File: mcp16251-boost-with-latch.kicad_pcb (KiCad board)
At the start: 2 copper layers, 28 parts, among them J1 THT_Castellated, J2 THT_Castellated, J3 THT_Castellated, J4 SMD_pad, J5 SMD_pad, J6 SMD_pad, J7 SMD_pad, J8 SMD_pad, J9 JST_PH_Header, Q1 Q_PMOS_GSD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

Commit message: Set design rules
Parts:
- moved R4 17.3 mm to (137.2, 96.5)
- moved R5 13.0 mm to (137.2, 101.6)
- moved SW2 13.0 mm to (134.6, 106.7)
- moved Q2 13.0 mm to (142.2, 101.6)
- moved R2 10.8 mm to (170.2, 87.8)
- moved R3 10.8 mm to (170.2, 94.0)
- moved RV1 10.8 mm to (172.7, 91.4)
- moved R1 10.2 mm to (139.7, 78.7)
- moved Q1 10.2 mm to (134.6, 78.7)
- moved C4 5.68 mm to (149.9, 85.5)
- moved C3 5.68 mm to (147.3, 85.5)
- turned U1 to 90 degrees
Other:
- net class Default: clearance 0.2 -> 0.2032; trace_width 0.25 -> 0.2032; via_dia 0.8 -> 0.6604; via_drill 0.4 -> 0.3302
- rule pad_to_mask_clearance: 0.051 -> 0.0508
- rule solder_mask_min_width: 0.25 -> 0.1778
- rule trace_clearance: 0.2 -> 0.2032
- rule trace_min: 0.2 -> 0.1778
- rule via_min_drill: 0.3 -> 0.3048
- rule via_min_size: 0.4 -> 0.6096
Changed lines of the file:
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@@
   )
   (layers
-    (0 F.Cu signal)
-    (31 B.Cu signal)
-    (32 B.Adhes user)
-    (33 F.Adhes user)
+    (0 F.Cu mixed)
+    (31 B.Cu mixed)
     (34 B.Paste user)
     (35 F.Paste user)
@@
   )
   (setup
-    (last_trace_width 0.25)
-    (trace_clearance 0.2)
+    (last_trace_width 0.2032)
+    (trace_clearance 0.2032)
     (zone_clearance 0.508)
     (zone_45_only no)
-    (trace_min 0.2)
+    (trace_min 0.1778)
     (segment_width 0.2)
     (edge_width 0.15)
-    (via_size 0.8)
-    (via_drill 0.4)
-    (via_min_size 0.4)
-    (via_min_drill 0.3)
+    (via_size 0.6604)
+    (via_drill 0.3302)
+    (via_min_size 0.6096)
+    (via_min_drill 0.3048)
     (uvia_size 0.3)
     (uvia_drill 0.1)
@@
     (pad_size 1.524 1.524)
     (pad_drill 0.762)
-    (pad_to_mask_clearance 0.051)
-    (solder_mask_min_width 0.25)
+    (pad_to_mask_clearance 0.0508)
+    (solder_mask_min_width 0.1778)
     (aux_axis_origin 0 0)
-    (visible_elements FFFFFF7F)
+    (visible_elements FFFFF77F)
     (pcbplotparams
       (layerselection 0x010fc_ffffffff)
@@
   (net 13 "Net-(SW1-Pad3)")
   (net_class Default "This is the default net class."
-    (clearance 0.2)
-    (trace_width 0.25)
-    (via_dia 0.8)
-    (via_drill 0.4)
+    (clearance 0.2032)
+    (trace_width 0.2032)
+    (via_dia 0.6604)
+    (via_drill 0.3302)
     (uvia_dia 0.3)
     (uvia_drill 0.1)
@@
   )
   (module MCP16251_module:R_1206_HS (layer F.Cu)
-    (at 142.24 88.01 270)
+    (at 147.32 85.47 270)
     (descr "Resistor SMD 1206, reflow soldering, Vishay (see dcrcw.pdf)")
     (tags "resistor 1206")
@@
   )
   (module MCP16251_module:R_1206_HS (layer F.Cu)
-    (at 144.78 88.01 270)
+    (at 149.86 85.47 270)
     (descr "Resistor SMD 1206, reflow soldering, Vishay (see dcrcw.pdf)")
     (tags "resistor 1206")
@@
   )
   (module MCP16251_module:SOT-23_HS (layer F.Cu)
-    (at 144.78 78.74 180)
+    (at 134.62 78.74 180)
     (descr "SOT-23, Standard")
     (tags SOT-23)
@@
   )
   (module MCP16251_module:SOT-23_HS (layer F.Cu)
-    (at 154.94 99.06)
+    (at 142.24 101.6)
     (descr "SOT-23, Standard")
     (tags SOT-23)
@@
   )
   (module MCP16251_module:R_0805_HS (layer F.Cu)
-    (at 149.86 78.74 270)
+    (at 139.7 78.74 270)
     (descr "Resistor SMD 0805, reflow soldering, Vishay (see dcrcw.pdf)")
     (tags "resistor 0805")
@@
   )
   (module MCP16251_module:R_0805_HS (layer F.Cu)
-    (at 162.56 80.13 270)
+    (at 170.18 87.75 270)
     (descr "Resistor SMD 0805, reflow soldering, Vishay (see dcrcw.pdf)")
     (tags "resistor 0805")
@@
   )
   (module MCP16251_module:R_0805_HS (layer F.Cu)
-    (at 162.56 86.36 270)
+    (at 170.18 93.98 270)
     (descr "Resistor SMD 0805, reflow soldering, Vishay (see dcrcw.pdf)")
     (tags "resistor 0805")
@@
   )
   (module MCP16251_module:R_0805_HS (layer F.Cu)
-    (at 152.666 88.961001)
+    (at 137.16 96.52)
     (descr "Resistor SMD 0805, reflow soldering, Vishay (see dcrcw.pdf)")
     (tags "resistor 0805")
@@
   )
   (module MCP16251_module:R_0805_HS (layer F.Cu)
-    (at 149.86 99.06)
+    (at 137.16 101.6)
     (descr "Resistor SMD 0805, reflow soldering, Vishay (see dcrcw.pdf)")
     (tags "resistor 0805")
@@
   )
   (module MCP16251_module:Conn_01x03_small (layer F.Cu)
-    (at 165.1 83.82)
+    (at 172.72 91.44)
     (fp_text reference RV1 (at 1.905 0 90) (layer F.SilkS)
       (effects (font (size 1 1) (thickness 0.15)))
@@
   )
   (module Buttons_Switches_SMD:SW_SPST_TL3342 (layer F.Cu)
-    (at 147.32 104.14)
+    (at 134.62 106.68)
     (descr "Low-profile SMD Tactile Switch, https://www.e-switch.com/system/asset/product_line/data_sheet/165/TL3342.pdf")
     (tags "SPST Tactile Switch")
@@
   )
   (module MCP16251_module:SOT-23-6_HS (layer F.Cu)
-    (at 156.18 84.77)
+    (at 156.18 84.77 90)
     (descr "6-pin SOT-23 package")
     (tags SOT-23-6)
     (attr smd)
-    (fp_text reference U1 (at 0 -2.54) (layer F.SilkS)
-      (effects (font (size 1 1) (thickness 0.15)))
-    )
-    (fp_text value MCP16251T (at 0 2.9) (layer F.Fab) hide
+    (fp_text reference U1 (at 0 -2.54 90) (layer F.SilkS)
+      (effects (font (size 1 1) (thickness 0.15)))
+    )
+    (fp_text value MCP16251T (at 0 2.9 90) (layer F.Fab) hide
       (effects (font (size 1 1) (thickness 0.15)))
     )
@@
     (fp_line (start 0.9 -1.61) (end -1.55 -1.61) (layer F.SilkS) (width 0.12))
     (fp_line (start -0.9 1.61) (end 0.9 1.61) (layer F.SilkS) (width 0.12))
-    (fp_text user %R (at 0 0 90) (layer F.Fab)
-      (effects (font (size 0.5 0.5) (thickness 0.075)))
-    )
-    (pad 5 smd roundrect (at 1.3 0) (size 1.46 0.65) (layers F.Cu F.Paste F.Mask) (roundrect_rratio 0.25)
+    (fp_text user %R (at 0 0 180) (layer F.Fab)
+      (effects (font (size 0.5 0.5) (thickness 0.075)))
+    )
+    (pad 5 smd roundrect (at 1.3 0 90) (size 1.46 0.65) (layers F.Cu F.Paste F.Mask) (roundrect_rratio 0.25)
       (net 1 VCC))
-    (pad 6 smd roundrect (at 1.3 -0.95) (size 1.46 0.65) (layers F.Cu F.Paste F.Mask) (roundrect_rratio 0.25)
+    (pad 6 smd roundrect (at 1.3 -0.95 90) (size 1.46 0.65) (layers F.Cu F.Paste F.Mask) (roundrect_rratio 0.25)
       (net 3 VBAT))
-    (pad 4 smd roundrect (at 1.3 0.95) (size 1.46 0.65) (layers F.Cu F.Paste F.Mask) (roundrect_rratio 0.25)
+    (pad 4 smd roundrect (at 1.3 0.95 90) (size 1.46 0.65) (layers F.Cu F.Paste F.Mask) (roundrect_rratio 0.25)
       (net 10 "Net-(R2-Pad2)"))
-    (pad 3 smd roundrect (at -1.3 0.95) (size 1.46 0.65) (layers F.Cu F.Paste F.Mask) (roundrect_rratio 0.25)
+    (pad 3 smd roundrect (at -1.3 0.95 90) (size 1.46 0.65) (layers F.Cu F.Paste F.Mask) (roundrect_rratio 0.25)
       (net 3 VBAT))
-    (pad 2 smd roundrect (at -1.3 0) (size 1.46 0.65) (layers F.Cu F.Paste F.Mask) (roundrect_rratio 0.25)
-      (net 2 GND))
-    (pad 1 smd roundrect (at -1.3 -0.95) (size 1.46 0.65) (layers F.Cu F.Paste F.Mask) (roundrect_rratio 0.25)
+    (pad 2 smd roundrect (at -1.3 0 90) (size 1.46 0.65) (layers F.Cu F.Paste F.Mask) (roundrect_rratio 0.25)
+      (net 2 GND))
+    (pad 1 smd roundrect (at -1.3 -0.95 90) (size 1.46 0.65) (layers F.Cu F.Paste F.Mask) (roundrect_rratio 0.25)
       (net 7 "Net-(L1-Pad2)"))
     (model ${KISYS3DMOD}/TO_SOT_Packages_SMD.3dshapes/SOT-23-6.wrl

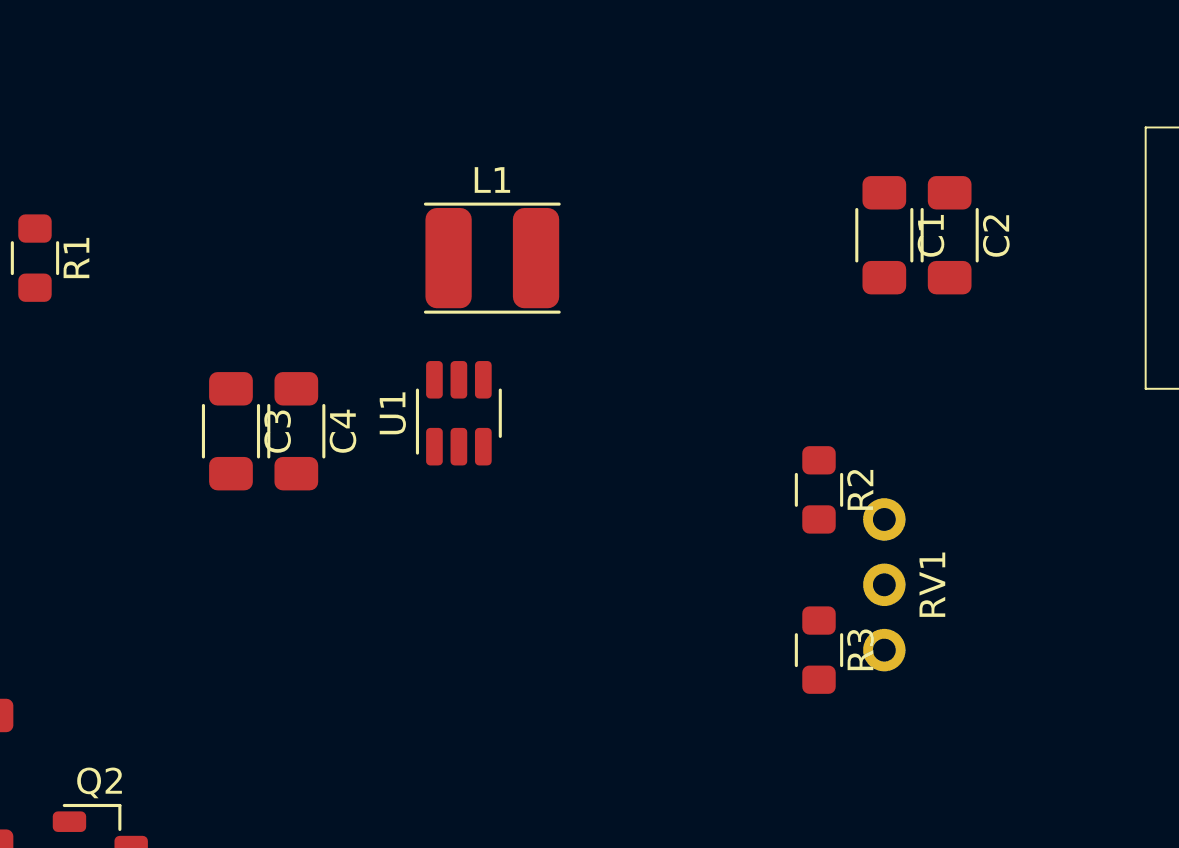
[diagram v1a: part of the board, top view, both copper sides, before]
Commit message: MCP16251 layout according to datasheet recommendation
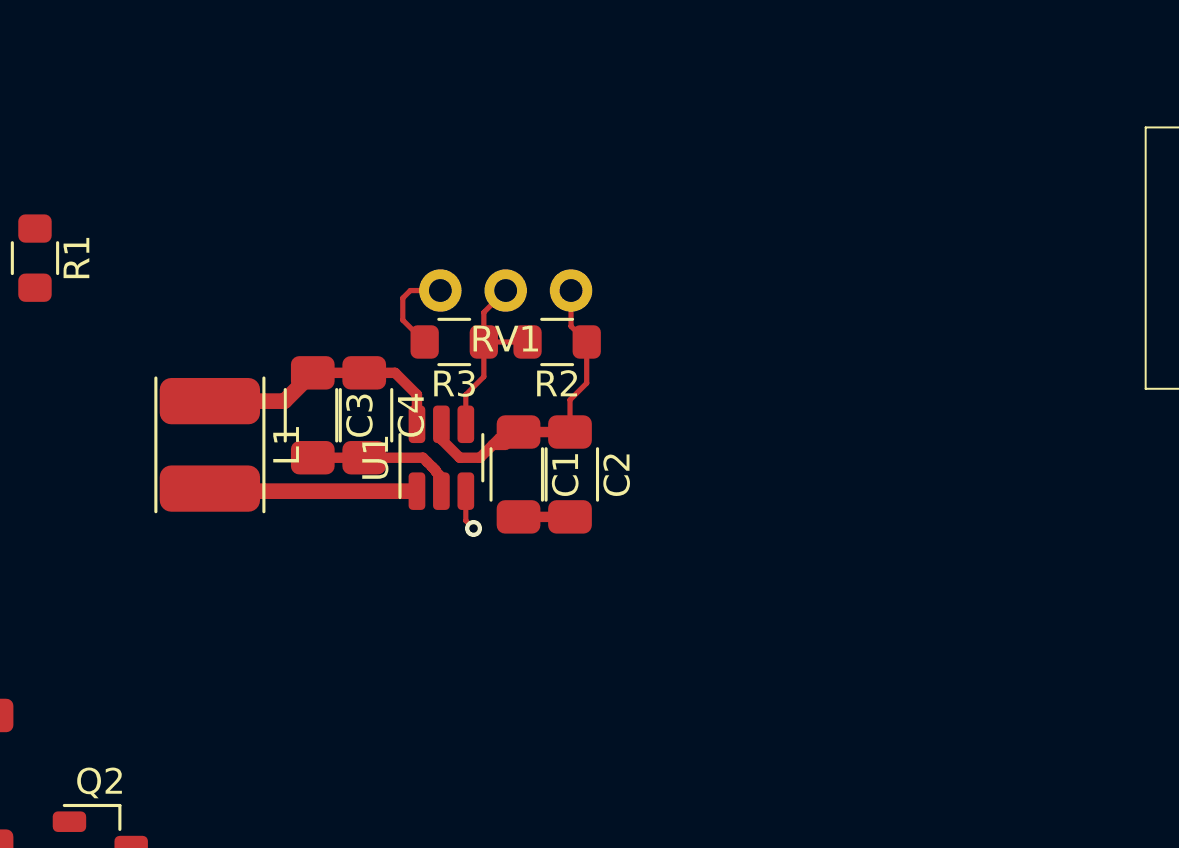
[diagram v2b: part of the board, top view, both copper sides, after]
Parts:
- moved RV1 18.6 mm to (158.0, 80.0), turned to 270 degrees
- moved R3 18.6 mm to (156.0, 82.0), turned to 180 degrees
- moved C2 17.4 mm to (160.5, 87.2)
- moved C1 17.0 mm to (158.5, 87.2)
- moved L1 13.2 mm to (146.5, 86.0), turned to 270 degrees
- moved R2 11.7 mm to (160.0, 82.0), turned to 180 degrees
- moved C3 3.24 mm to (150.5, 84.8)
- moved C4 2.71 mm to (152.5, 84.8)
- moved U1 1.86 mm to (155.5, 86.5)
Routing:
- net VCC: track 0.00 -> 12.2 mm
- net VBAT: track 0.00 -> 11.6 mm, vias 0 -> 1
- net GND: track 0.00 -> 11.1 mm
- net Net-(L1-Pad2): track 0.00 -> 8.09 mm
- net Net-(R2-Pad2): track 0.00 -> 7.54 mm
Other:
- net class Wide_16mil added: clearance 0.2032, trace_width 0.4064, via_dia 0.7112, via_drill 0.3556

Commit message: Further layout
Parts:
- moved J2 20.7 mm to (170.2, 82.5)
- moved J6 20.5 mm to (167.6, 91.4)
- moved J8 20.5 mm to (167.6, 94.0)
- moved SW2 18.0 mm to (147.3, 94.0), turned to 180 degrees
- moved Q2 15.3 mm to (141.0, 86.4)
- moved JP1 14.3 mm to (141.5, 79.0)
- moved SW1 13.1 mm to (140.0, 81.5)
- moved Q1 11.5 mm to (146.0, 80.5), turned to 270 degrees
- moved R1 10.9 mm to (150.5, 80.0), turned to 0 degrees
- moved R4 10.2 mm to (137.2, 86.4), turned to 90 degrees
- moved J1 9.67 mm to (127.0, 82.5)
- moved R5 9.67 mm to (141.0, 92.7), turned to 90 degrees
- moved J5 9.16 mm to (137.2, 91.4)
- moved J7 8.03 mm to (137.2, 94.0)
- moved J9 7.73 mm to (132.1, 90.2)
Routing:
- net Vbat_raw_sense: track 0.00 -> 10.4 mm
- net Net-(Q1-Pad1): track 0.00 -> 5.32 mm
- net VBAT: track 11.6 -> 14.5 mm
- net VBAT_RAW: track 0.00 -> 2.64 mm

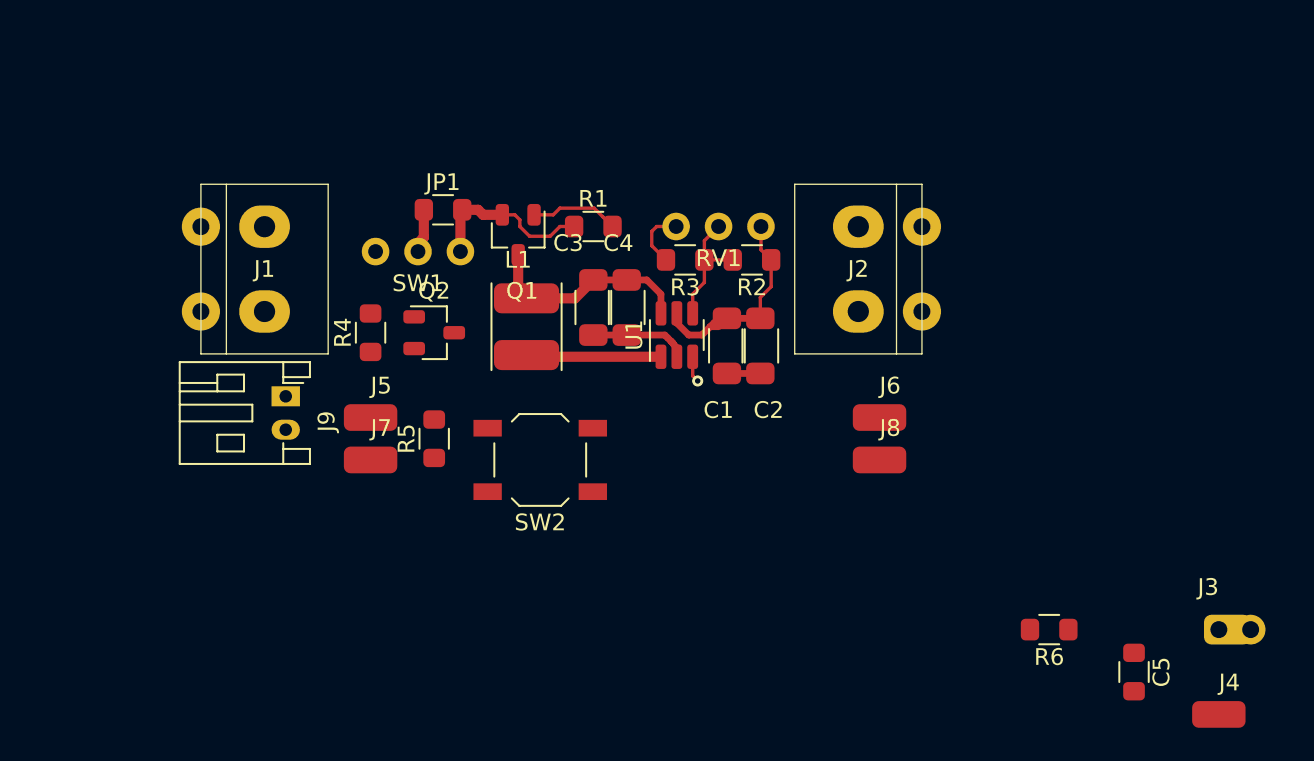
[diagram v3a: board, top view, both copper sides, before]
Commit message: Try alternative (more square-ish) layout
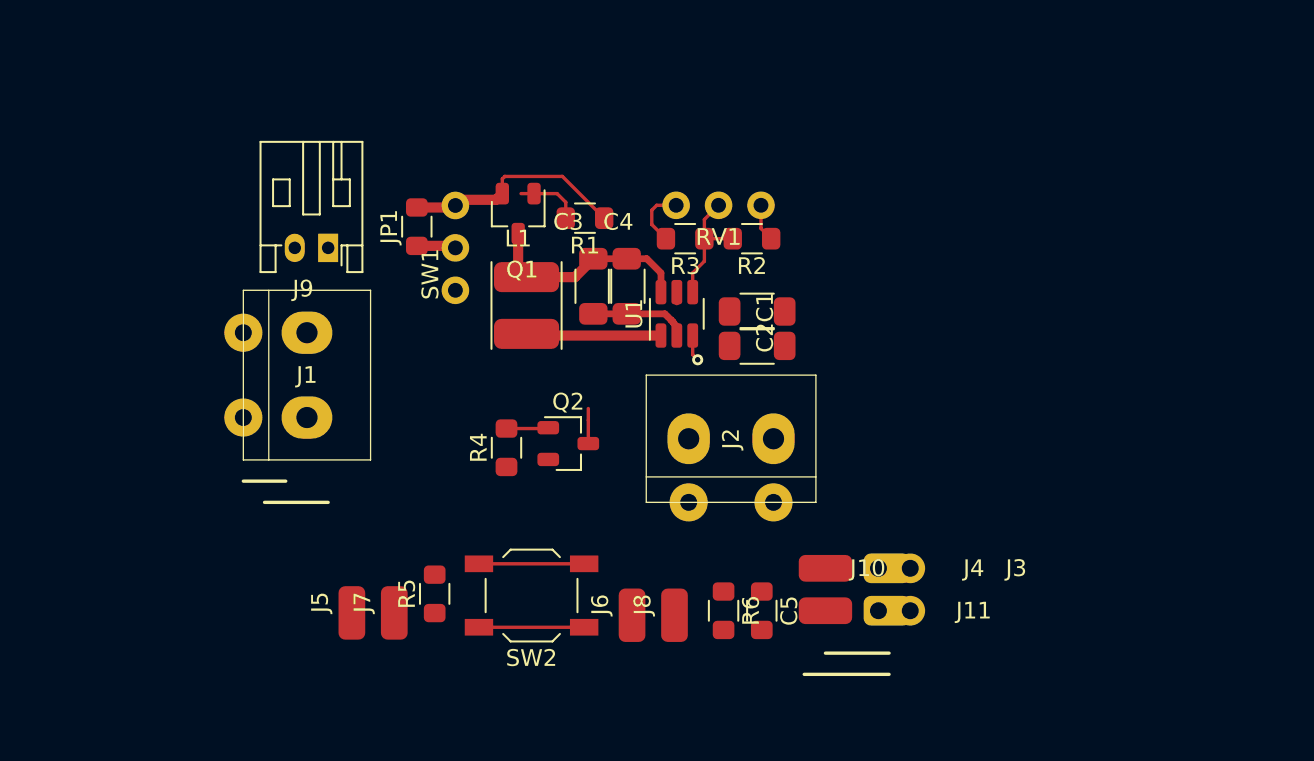
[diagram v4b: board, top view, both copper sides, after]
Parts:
- added J10: THT_Castellated, MCP16251_module:Conn_01x01_cast, F.Cu at (169.5, 103.0)
- added J11: SMD_pad, MCP16251_module:SMD-Pad_01x01, F.Cu at (164.4, 103.0)
- moved J4 25.1 mm to (164.4, 100.5)
- moved C5 22.6 mm to (160.6, 103.0)
- moved J3 20.7 mm to (169.5, 100.5)
- moved R6 19.5 mm to (158.3, 103.0), turned to 270 degrees
- moved J6 19.0 mm to (152.8, 103.3), turned to 90 degrees
- moved J2 18.1 mm to (158.8, 96.5), turned to 270 degrees
- moved J8 15.4 mm to (155.4, 103.3), turned to 90 degrees
- moved J5 11.8 mm to (136.0, 103.1), turned to 90 degrees
- moved R4 10.7 mm to (145.3, 93.2)
- moved Q2 10.4 mm to (149.0, 93.0)
- moved R5 9.29 mm to (141.0, 102.0)
- moved J7 9.27 mm to (138.6, 103.1), turned to 90 degrees
- moved J9 9.25 mm to (134.6, 81.3), turned to 180 degrees
- moved SW2 8.14 mm to (146.8, 102.1)
- moved J1 6.84 mm to (129.5, 88.9)
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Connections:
- J2 pad 1: VCC -> GND
- J2 pad 2: GND -> VCC
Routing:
- net VCC: track 12.2 -> 2.84 mm
- net Net-(Q1-Pad1): track 5.32 -> 12.2 mm
- net Net-(R5-Pad1): track 0.00 -> 6.30 mm
- net Vbat_raw_sense: track 10.4 -> 13.5 mm
- net Net-(Q2-Pad1): track 0.00 -> 2.52 mm
- net GND: track 11.1 -> 9.12 mm

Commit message: Completed alternative layout. Size 1.3in x 0.9in
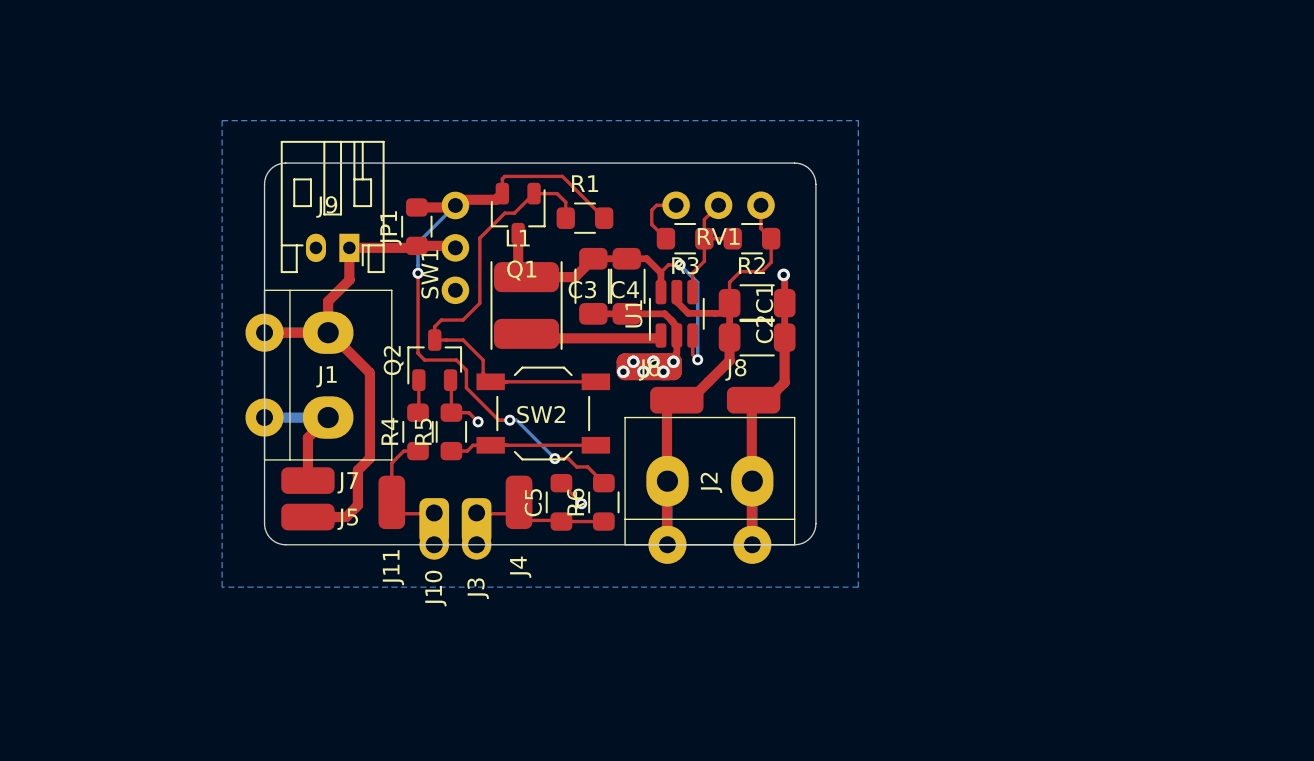
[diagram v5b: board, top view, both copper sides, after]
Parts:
- moved J10 28.8 mm to (141.0, 99.1), turned to 90 degrees
- moved J11 26.8 mm to (138.4, 96.5), turned to 270 degrees
- moved J3 26.0 mm to (143.5, 99.1), turned to 90 degrees
- moved J4 18.8 mm to (146.1, 96.5), turned to 90 degrees
- moved J8 13.7 mm to (160.1, 90.4), turned to 0 degrees
- moved C5 13.6 mm to (148.6, 96.5), turned to 90 degrees
- moved J6 13.2 mm to (155.5, 90.4), turned to 0 degrees
- moved SW2 10.9 mm to (147.5, 91.2)
- moved R5 9.75 mm to (142.0, 92.3)
- moved R6 9.67 mm to (151.1, 96.5), turned to 90 degrees
- moved J7 9.46 mm to (133.4, 95.2), turned to 180 degrees
- moved Q2 9.43 mm to (141.0, 88.0), turned to 90 degrees
- moved J5 6.31 mm to (133.4, 97.4), turned to 180 degrees
- moved R4 5.38 mm to (140.0, 92.3)
- moved J2 2.84 mm to (157.5, 99.1)
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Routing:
- net GND: track 9.12 -> 53.0 mm, vias 0 -> 9
- net VBAT_RAW: track 2.36 -> 34.1 mm
- net VCC: track 2.84 -> 30.5 mm
- net Vbat_raw_sense: track 13.5 -> 38.3 mm, vias 0 -> 3
- net Net-(Q1-Pad1): track 12.2 -> 26.8 mm
- net Net-(C5-Pad1): track 0.00 -> 9.28 mm
- net PWR_CONTROL: track 0.00 -> 7.61 mm
- net VBAT: track 14.5 -> 22.0 mm, vias 1 -> 2
- net Net-(R5-Pad1): track 6.30 -> 9.79 mm
- added copper zone on B.Cu, net GND
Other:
- board outline added: 33 x 22.9 mm
- net class Wide_16mil: via_dia 0.7112 -> 0.762; via_drill 0.3556 -> 0.381
